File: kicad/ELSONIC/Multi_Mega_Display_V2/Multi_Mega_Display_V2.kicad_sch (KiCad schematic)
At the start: 44 parts, among them J1 Conn_02x10_Odd_Even, Q1 KRC105S, U1 74HCT574, U2 74HCT574

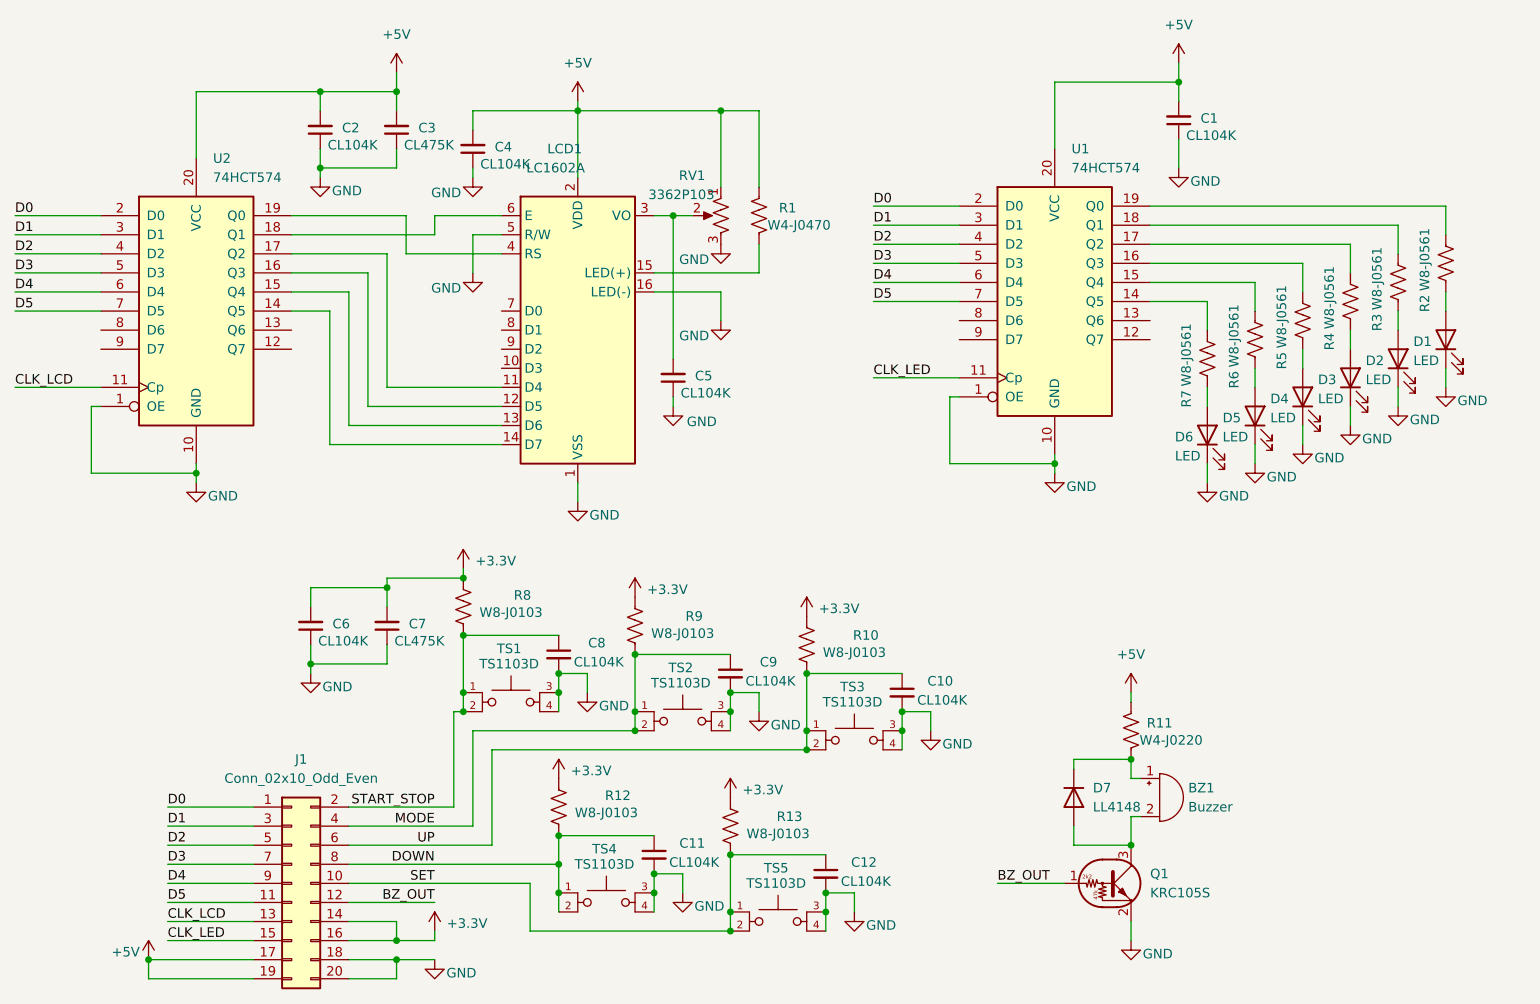
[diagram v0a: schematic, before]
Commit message: chore: KiCad 아트웍 및 라이브러리 변경 반영
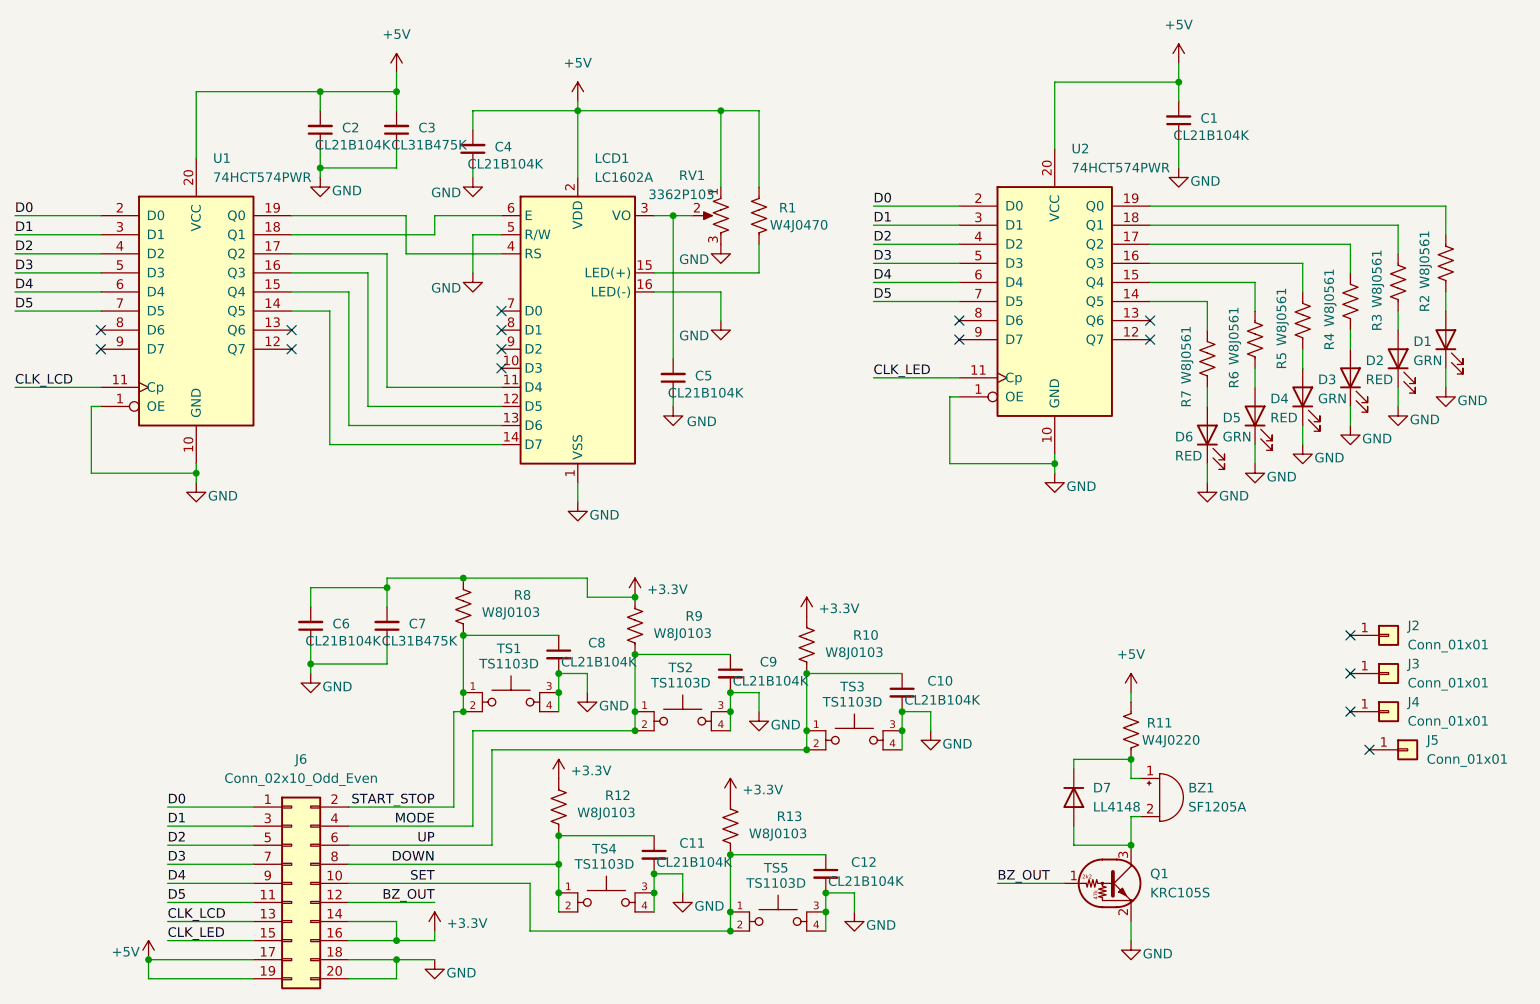
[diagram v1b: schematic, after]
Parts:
- removed J1: Conn_02x10_Odd_Even, symbol Connector_Generic:Conn_02x10_Odd_Even
- removed LCD1: LC1602A, Display:WC1602A, symbol Display_Character:WC1602A
- removed U1, U2: 74HCT574, symbol 74xx:74HCT574
- added J2, J3, J4, J5: Conn_01x01, 06_MyFoot_Mechanical:MTHole_3.5mm_7.5mmPad_GND, symbol Connector_Generic:Conn_01x01
- added J6: Conn_02x10_Odd_Even, 02_MyFoot_Connectors:IDC-Header_2x10_P2.54mm_Vertical, symbol 02_MyLib_Connectors:Conn_02x10_Odd_Even
- added LCD1: LC1602A, 06_MyFoot_Mechanical:LC1602A, symbol 05_MyLib_Others:LC1602A
- added U1, U2: 74HCT574PWR, 01_MyFoot_ICs:TSSOP-20_4.4x6.5mm_P0.65mm, symbol 01_MyLib_ICs:74HCT574
- BZ1: value Buzzer -> SF1205A; footprint (none) -> 03_MyFoot_Active:Buzzer_12x9.5RM7.6
- C1, C10, C11, C12, C2, C4, C5, C6, C8, C9: value CL104K -> CL21B104K; LCSC (none) -> C1711
- C3, C7: value CL475K -> CL31B475K; footprint 04_MyFoot_Passive:C_2012Metric -> 04_MyFoot_Passive:C_3216Metric; LCSC (none) -> C1872
- D1: value LED -> GRN; footprint (none) -> 03_MyFoot_Active:LED_NORMAL
- D2: value LED -> RED; footprint (none) -> 03_MyFoot_Active:LED_H_LSET
- D3: value LED -> GRN; footprint (none) -> 03_MyFoot_Active:LED_8POWER
- D4: value LED -> RED; footprint (none) -> 03_MyFoot_Active:LED_REMOTE
- D5: value LED -> GRN; footprint (none) -> 03_MyFoot_Active:LED_EXT
- D6: value LED -> RED; footprint (none) -> 03_MyFoot_Active:LED_TXRX
- D7: footprint (none) -> 03_MyFoot_Active:LL4148_MELF; LCSC (none) -> C68883
- Q1: footprint (none) -> 03_MyFoot_Active:SOT-23_KRC105S; LCSC (none) -> C112793
- R1: value W4-J0470 -> W4J0470; footprint 04_MyFoot_Passive:R_2012Metric -> 04_MyFoot_Passive:R_3216Metric; LCSC (none) -> C25384
- R10, R12, R13, R8, R9: value W8-J0103 -> W8J0103; LCSC (none) -> C25612
- R11: value W4-J0220 -> W4J0220; footprint 04_MyFoot_Passive:R_2012Metric -> 04_MyFoot_Passive:R_3216Metric; LCSC (none) -> C25364
- R2, R3, R4, R5, R6, R7: value W8-J0561 -> W8J0561; LCSC (none) -> C25319
- RV1: footprint (none) -> 04_MyFoot_Passive:TRIM_3362P
- TS1, TS2, TS3, TS4, TS5: footprint (none) -> 06_MyFoot_Mechanical:SW_PUSH-12mm
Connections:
- net +3.3V: now also J6.14 (Pin_14), J6.16 (Pin_16)
- net +5V: now also J6.17 (Pin_17), J6.19 (Pin_19), LCD1.2 (VDD), U1.20 (VCC), U2.20 (VCC)
- net BZ_OUT: now also J6.12 (Pin_12)
- net CLK_LCD: now also J6.13 (Pin_13), U1.11 (Cp)
- net CLK_LED: now also J6.15 (Pin_15), U2.11 (Cp)
- net D0: now also J6.1 (Pin_1), U1.2 (D0), U2.2 (D0)
- net D1: now also J6.3 (Pin_3), U1.3 (D1), U2.3 (D1)
- net D2: now also J6.5 (Pin_5), U1.4 (D2), U2.4 (D2)
- net D3: now also J6.7 (Pin_7), U1.5 (D3), U2.5 (D3)
- net D4: now also J6.9 (Pin_9), U1.6 (D4), U2.6 (D4)
- net D5: now also J6.11 (Pin_11), U1.7 (D5), U2.7 (D5)
- net DOWN: now also J6.8 (Pin_8)
- net GND: now also J6.18 (Pin_18), J6.20 (Pin_20), LCD1.1 (VSS), LCD1.16 (LED(-)), LCD1.5 (R/W), U1.1 (OE), U1.10 (GND), U2.1 (OE), U2.10 (GND)
- net MODE: now also J6.4 (Pin_4)
- net SET: now also J6.10 (Pin_10)
- net START_STOP: now also J6.2 (Pin_2)
- net UP: now also J6.6 (Pin_6)
- net at C5.2, RV1.2: now also LCD1.3 (VO)
- net at R5.2: now also U2.16 (Q3)
- net at R1.1: now also LCD1.15 (LED(+))
- net at R4.2: now also U2.17 (Q2)
- net at R7.2: now also U2.14 (Q5)
- net at R6.2: now also U2.15 (Q4)
- net at R3.2: now also U2.18 (Q1)
- net at R2.2: now also U2.19 (Q0)
- new net: LCD1.11 (D4), U1.17 (Q2)
- new net: LCD1.12 (D5), U1.16 (Q3)
- new net: LCD1.13 (D6), U1.15 (Q4)
- new net: LCD1.14 (D7), U1.14 (Q5)
- new net: LCD1.4 (RS), U1.19 (Q0)
- new net: LCD1.6 (E), U1.18 (Q1)
- no-connect marks 0 -> 16
